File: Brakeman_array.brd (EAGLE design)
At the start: 103.6 x 99.1 mm, 72 parts

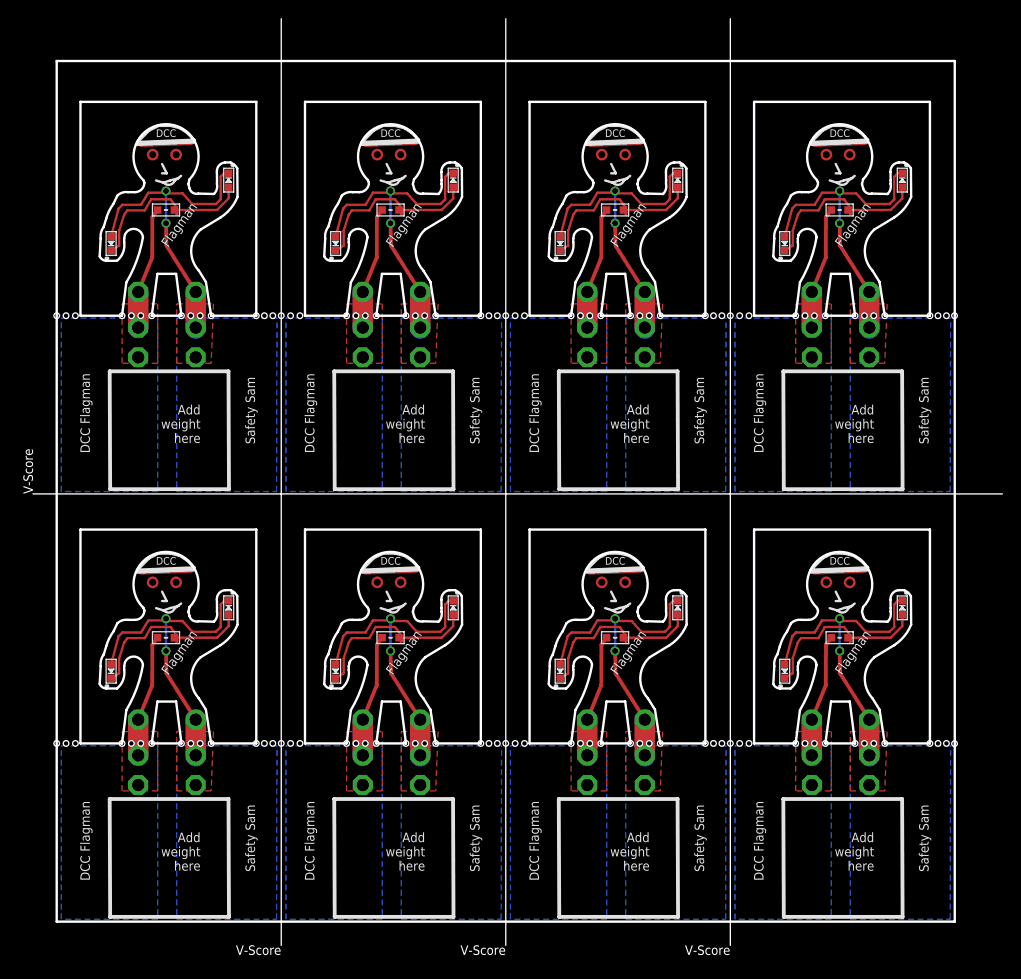
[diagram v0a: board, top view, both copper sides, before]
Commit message: fixed silkscreen/layer issues with PCBWay
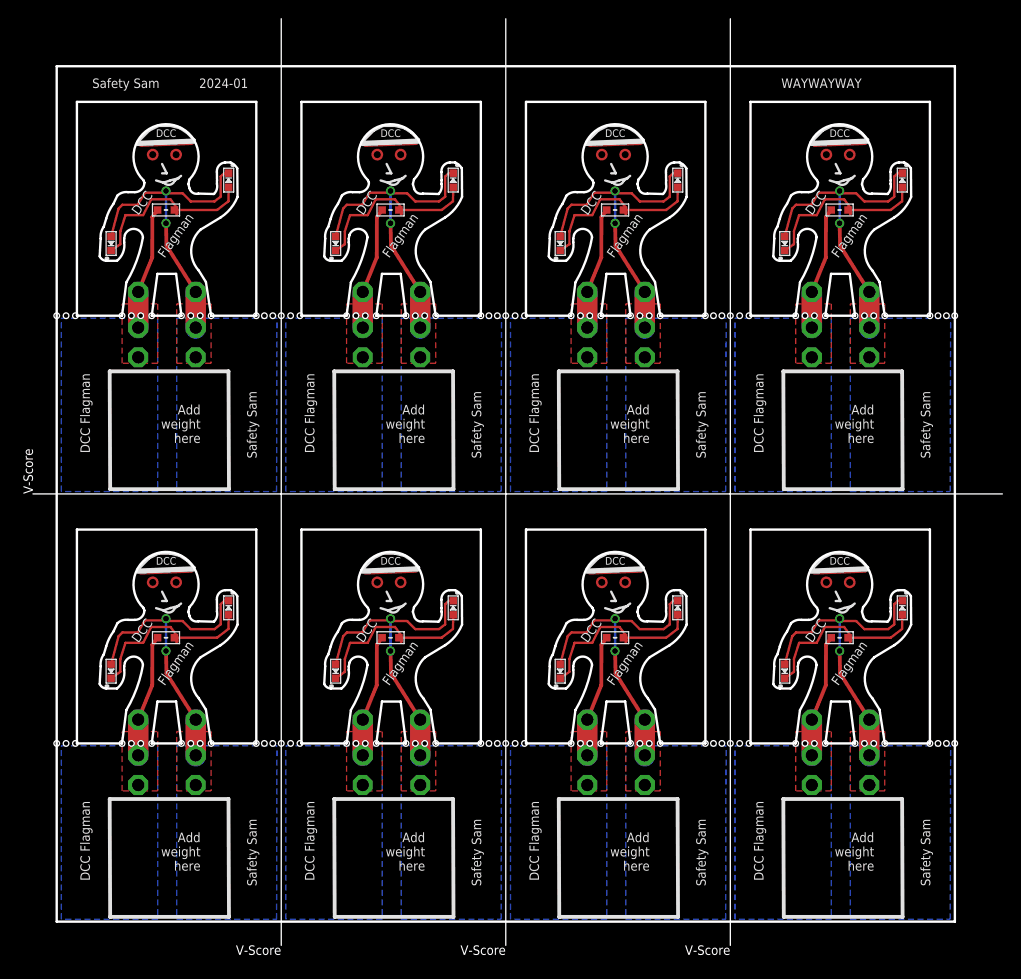
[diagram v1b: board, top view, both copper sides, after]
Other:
- outline, holes or cut-outs redrawn
- board text added: "2024-01"
- board text added: "WAYWAYWAY"
